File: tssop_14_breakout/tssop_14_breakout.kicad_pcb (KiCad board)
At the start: 2 copper layers, 17 x 20 mm, 4 parts, among them J7 tssop_14_left, J8 tssop_14_right, U4 tssop-14

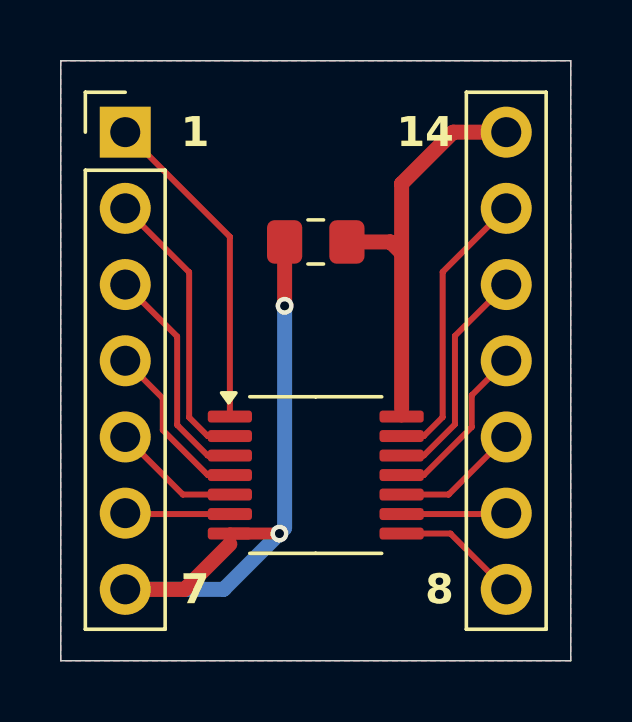
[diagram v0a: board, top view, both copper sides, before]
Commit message: added DFN breakout changed trim pot type in 33063_boost, 33063_invert, r1283_power boards fixed error in 33063_boost board (move trim pot to higher side of voltage divider)
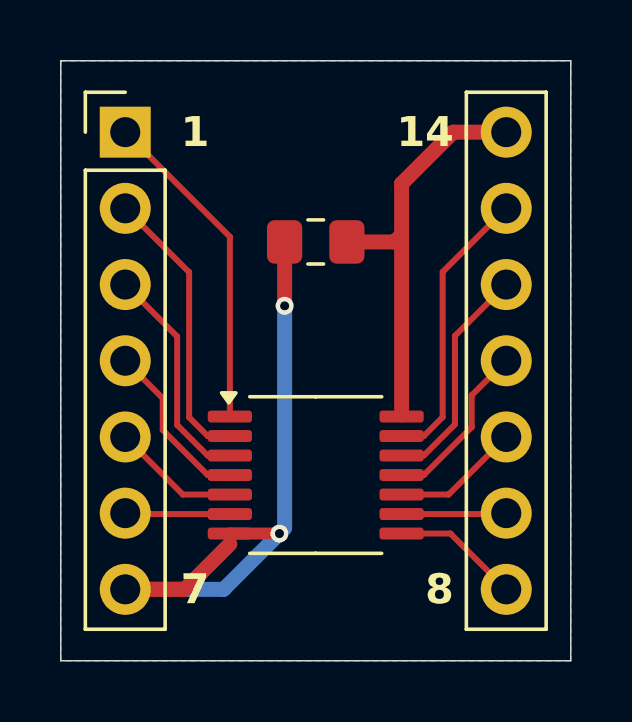
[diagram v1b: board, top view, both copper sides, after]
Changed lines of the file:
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@@
 	)
 	(segment
-		(start 61.3625 61.6225)
-		(end 61.3625 54.0975)
-		(width 0.5)
+		(start 61.3625 61.86)
+		(end 61.3625 61.6225)
+		(width 0.4)
 		(layer "F.Cu")
 		(net 2)
@@
 		(start 63.08 52.38)
 		(end 64.85 52.38)
-		(width 0.5)
-		(layer "F.Cu")
-		(net 2)
-	)
-	(segment
-		(start 61.3625 56.41)
-		(end 60.9925 56.04)
 		(width 0.5)
 		(layer "F.Cu")
@@
 	)
 	(segment
-		(start 61.3625 61.86)
-		(end 61.3625 61.6225)
-		(width 0.4)
+		(start 61.3625 55.8)
+		(end 61.1225 56.04)
+		(width 0.5)
 		(layer "F.Cu")
 		(net 2)
 	)
 	(segment
-		(start 60.9925 56.04)
+		(start 61.1225 56.04)
 		(end 59.5375 56.04)
 		(width 0.5)
 		(layer "F.Cu")
+		(net 2)
+	)
+	(segment
+		(start 61.3625 55.8)
+		(end 61.3625 54.0975)
+		(width 0.5)
+		(layer "F.Cu")
+		(net 2)
+	)
+	(segment
+		(start 61.3625 61.6225)
+		(end 61.3625 55.8)
+		(width 0.5)
+		(layer "F.Cu")
